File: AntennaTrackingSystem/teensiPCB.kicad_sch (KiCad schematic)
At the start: 13 parts, among them J1 screw terminal, J2 Conn_01x02, J5 UART1, J6 UART2, J7 I2C ext, SW1 SW_Push, U2 SAM-M10Q-00B

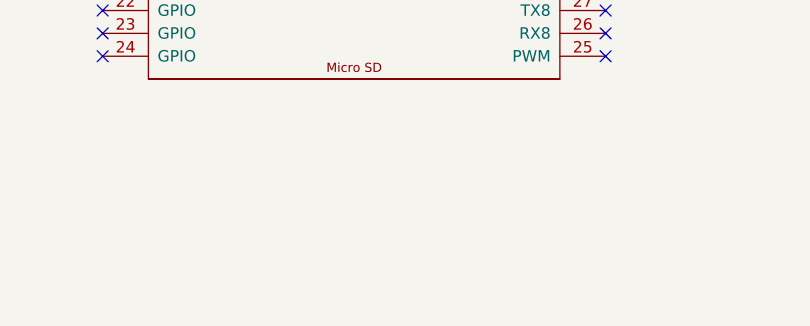
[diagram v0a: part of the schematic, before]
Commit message: moutning holes and corrections
added mounting holes, still would want a better footprint for the teensy
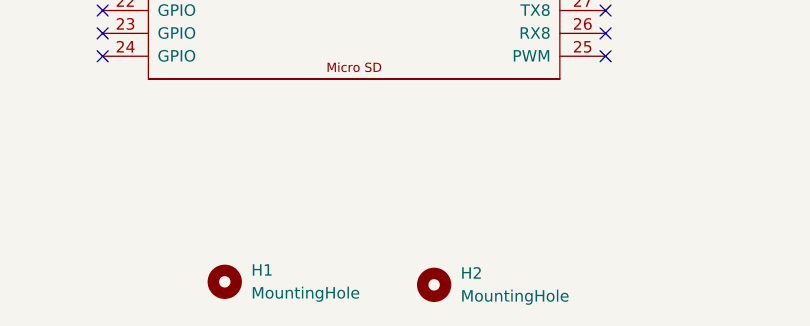
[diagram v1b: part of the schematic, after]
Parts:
- added H1, H2: MountingHole, MountingHole:MountingHole_3.2mm_M3, symbol Mechanical:MountingHole
- U2: footprint SAM M10Q footprint:SAM-M10Q_UBL -> SAM-M10Q:SAM-M10Q_UBL
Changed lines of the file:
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@@
+	)
+	(symbol
+		(lib_id "Mechanical:MountingHole")
+		(at 69.4444 136.8234 0)
+		(unit 1)
+		(body_style 1)
+		(exclude_from_sim no)
+		(in_bom no)
+		(on_board yes)
+		(in_pos_files yes)
+		(dnp no)
+		(fields_autoplaced yes)
+		(property "Reference" "H1"
+			(at 72.39 135.5533 0)
+			(show_name no)
+			(do_not_autoplace no)
+			(effects
+				(font
+					(size 1.27 1.27)
+				)
+				(justify left)
+			)
+		)
+		(property "Value" "MountingHole"
+			(at 72.39 138.0933 0)
+			(show_name no)
+			(do_not_autoplace no)
+			(effects
+				(font
+					(size 1.27 1.27)
+				)
+				(justify left)
+			)
+		)
+		(property "Footprint" "MountingHole:MountingHole_3.2mm_M3"
+			(at 69.4444 136.8234 0)
+			(hide yes)
+			(show_name no)
+			(do_not_autoplace no)
+			(effects
+				(font
+					(size 1.27 1.27)
+				)
+			)
+		)
+		(property "Datasheet" ""
+			(at 69.4444 136.8234 0)
+			(hide yes)
+			(show_name no)
+			(do_not_autoplace no)
+			(effects
+				(font
+					(size 1.27 1.27)
+				)
+			)
+		)
+		(property "Description" "Mounting Hole without connection"
+			(at 69.4444 136.8234 0)
+			(hide yes)
+			(show_name no)
+			(do_not_autoplace no)
+			(effects
+				(font
+					(size 1.27 1.27)
+				)
+			)
+		)
+		(instances
+			(project "teensiPCB"
+				(path "/ba786cef-8ef6-45a2-be74-19524883f146"
+					(reference "H1")
+					(unit 1)
+				)
+			)
+		)
 	)
 	(symbol
@@
 			)
 		)
-		(property "Footprint" "SAM M10Q footprint:SAM-M10Q_UBL"
+		(property "Footprint" "SAM-M10Q:SAM-M10Q_UBL"
 			(at 161.29 55.88 0)
 			(hide yes)
@@
 					(unit 1)
 				)
+			)
+		)
+	)
+	(symbol
+		(lib_id "Mechanical:MountingHole")
+		(at 92.71 137.16 0)
+		(unit 1)
+		(body_style 1)
+		(exclude_from_sim no)
+		(in_bom no)
+		(on_board yes)
+		(in_pos_files yes)
+		(dnp no)
+		(fields_autoplaced yes)
+		(property "Reference" "H2"
+			(at 95.6556 135.8899 0)
+			(show_name no)
+			(do_not_autoplace no)
+			(effects
+				(font
+					(size 1.27 1.27)
+				)
+				(justify left)
+			)
+		)
+		(property "Value" "MountingHole"
+			(at 95.6556 138.4299 0)
+			(show_name no)
+			(do_not_autoplace no)
+			(effects
+				(font
+					(size 1.27 1.27)
+				)
+				(justify left)
+			)
+		)
+		(property "Footprint" "MountingHole:MountingHole_3.2mm_M3"
+			(at 92.71 137.16 0)
+			(hide yes)
+			(show_name no)
+			(do_not_autoplace no)
+			(effects
+				(font
+					(size 1.27 1.27)
+				)
+			)
+		)
+		(property "Datasheet" ""
+			(at 92.71 137.16 0)
+			(hide yes)
+			(show_name no)
+			(do_not_autoplace no)
+			(effects
+				(font
+					(size 1.27 1.27)
+				)
+			)
+		)
+		(property "Description" "Mounting Hole without connection"
+			(at 92.71 137.16 0)
+			(hide yes)
+			(show_name no)
+			(do_not_autoplace no)
+			(effects
+				(font
+					(size 1.27 1.27)
+				)
+			)
+		)
+		(instances
+			(project "teensiPCB"
+				(path "/ba786cef-8ef6-45a2-be74-19524883f146"
+					(reference "H2")
+					(unit 1)
+				)

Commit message: teensy footprint
I have placed the correct teensy footprint that I got from the SRAD-Avionics Apollo folder
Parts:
- Ue1: footprint avionicsKiCadLibrary:Teensy41 -> teensy:teensy
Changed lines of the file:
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@@
 			)
 		)
-		(property "Footprint" "avionicsKiCadLibrary:Teensy41"
+		(property "Footprint" "teensy:teensy"
 			(at 73.66 97.79 0)
 			(hide yes)
